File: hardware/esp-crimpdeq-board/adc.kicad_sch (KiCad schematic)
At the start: 11 parts, among them IC1 ADS1235IRHBT, IC3 ADS1230IPWR

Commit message: Added 5V to ADC
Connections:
- net GND: now also IC1.5 (AVSS)
- net +5V: now reaches IC1.27 (AIN3), IC1.28 (AIN2), IC1.30 (AIN0)
- net +5V: now also IC1.29 (AIN1), IC1.4 (AVDD)

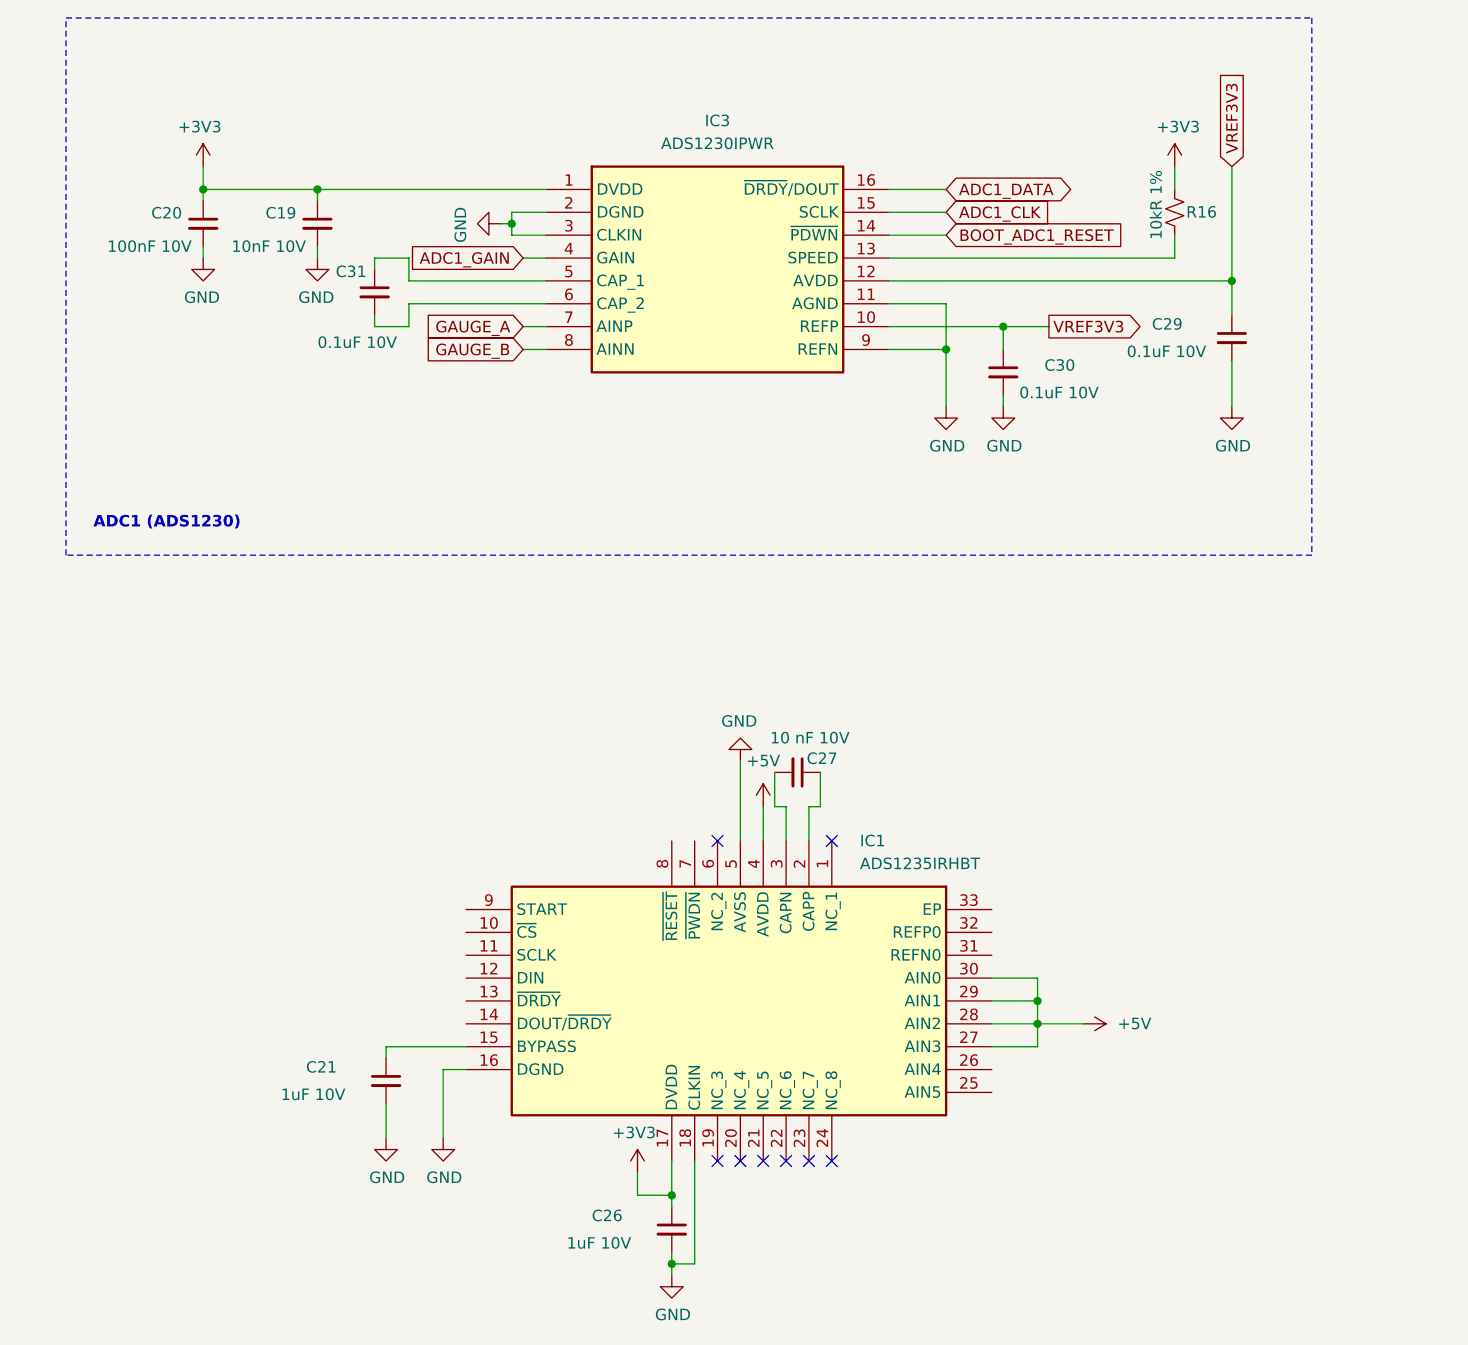
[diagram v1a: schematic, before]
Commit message: Ordering sdchematic in different sheets
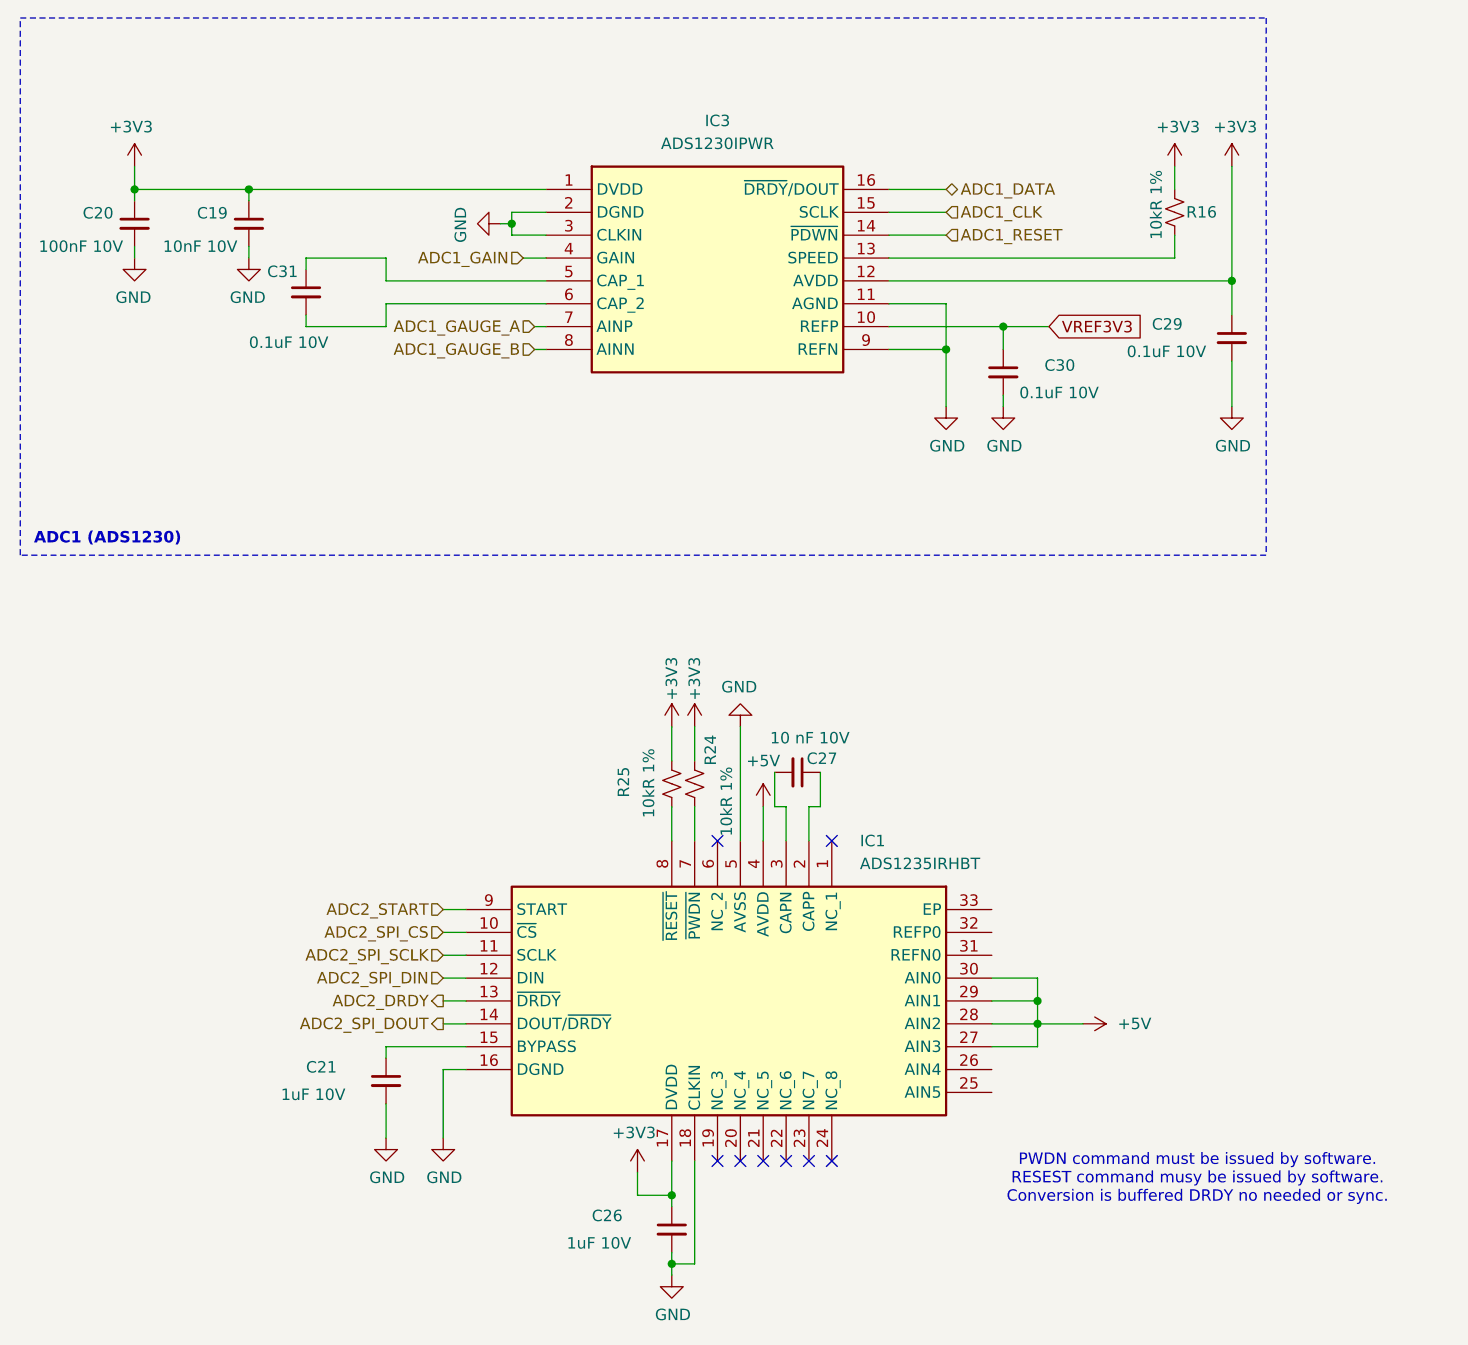
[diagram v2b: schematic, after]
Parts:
- added R24, R25: 10kR 1%, Resistor_SMD:R_0402_1005Metric, symbol Device:R_Small_US
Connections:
- net +3V3: now also C29.1, IC3.12 (AVDD), R24.1, R25.1
- net VREF3V3: no longer C29.1, IC3.12 (AVDD)
- net ADC2_SPI_CS: now reaches IC1.10 (~{CS})
- net ADC2_SPI_SCLK: now reaches IC1.11 (SCLK)
- net ADC2_SPI_DIN: now reaches IC1.12 (DIN)
- net ADC2_DRDY: now reaches IC1.13 (~{DRDY})
- net ADC2_SPI_DOUT: now reaches IC1.14 (DOUT/~{DRDY})
- net at IC1.7 (~{PWDN}): now also R24.2
- net at IC1.8 (~{RESET}): now also R25.2
- net ADC2_START: now reaches IC1.9 (START)
- net BOOT_ADC1_RESET renamed ADC1_RESET
- net GAUGE_A renamed ADC1_GAUGE_A
- net GAUGE_B renamed ADC1_GAUGE_B
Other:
- note added: "PWDN command must be issued by software. RESEST command musy be issued by software. Conversion is buffered DRDY no needed or sync."
- moved on the sheet: C19, C20, C31

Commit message: feat: Organice schematic
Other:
- note added: "ADC2 (ADS1235)"
- moved on the sheet: C21, C26, C27, IC1, R24, R25
